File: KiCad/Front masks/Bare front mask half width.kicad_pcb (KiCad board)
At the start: 2 copper layers, 17.6 x 111.5 mm, 3 parts

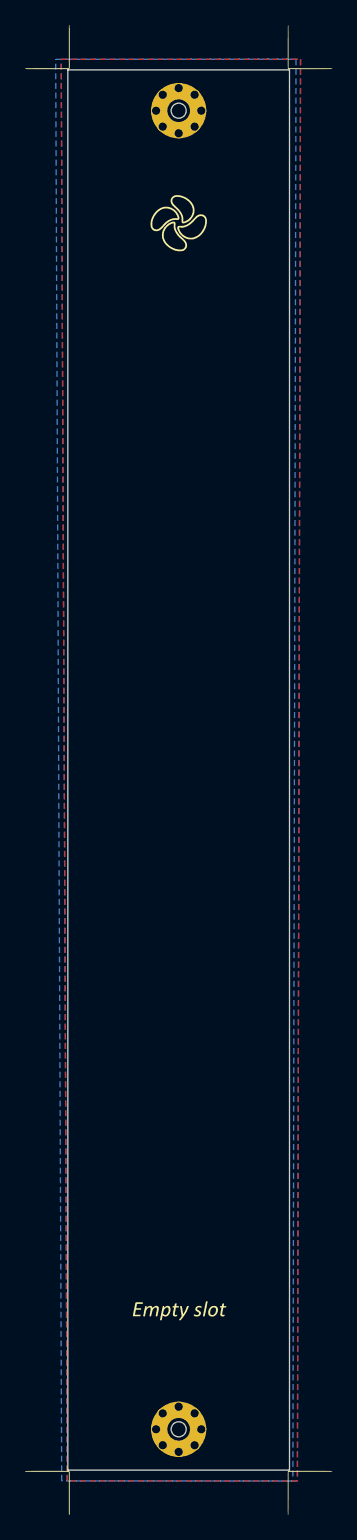
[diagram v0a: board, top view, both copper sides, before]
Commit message: BOM update (knob), mechanical folder added
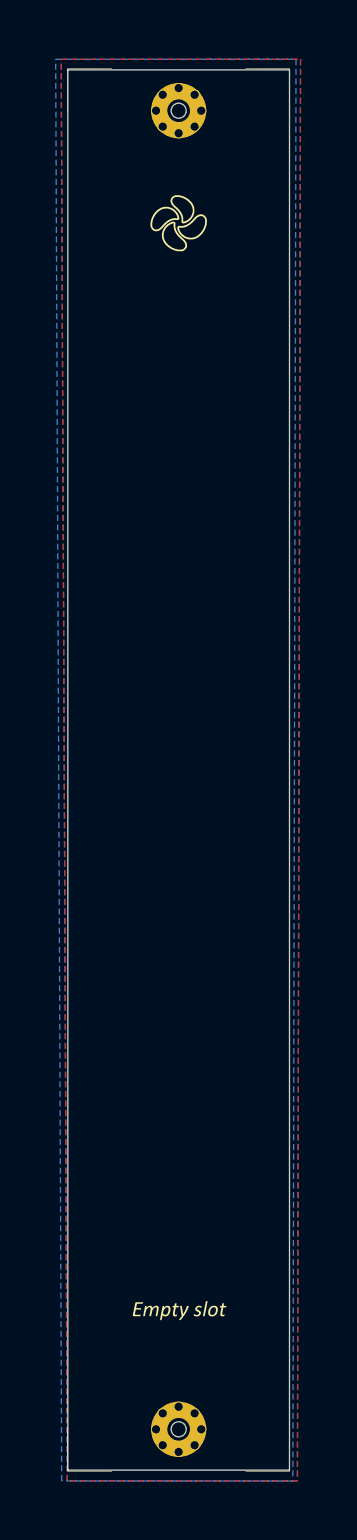
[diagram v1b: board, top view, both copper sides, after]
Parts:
- moved G*** 0.91 mm to (149.1, 94.2)
